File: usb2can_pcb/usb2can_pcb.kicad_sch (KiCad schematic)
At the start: 19 parts, among them J1 USB_C_Receptacle_USB2.0, J2 CAN, J3 CAN, U1 XC6206P332MR, U2 STM32F072C8T6, U3 MAX3051

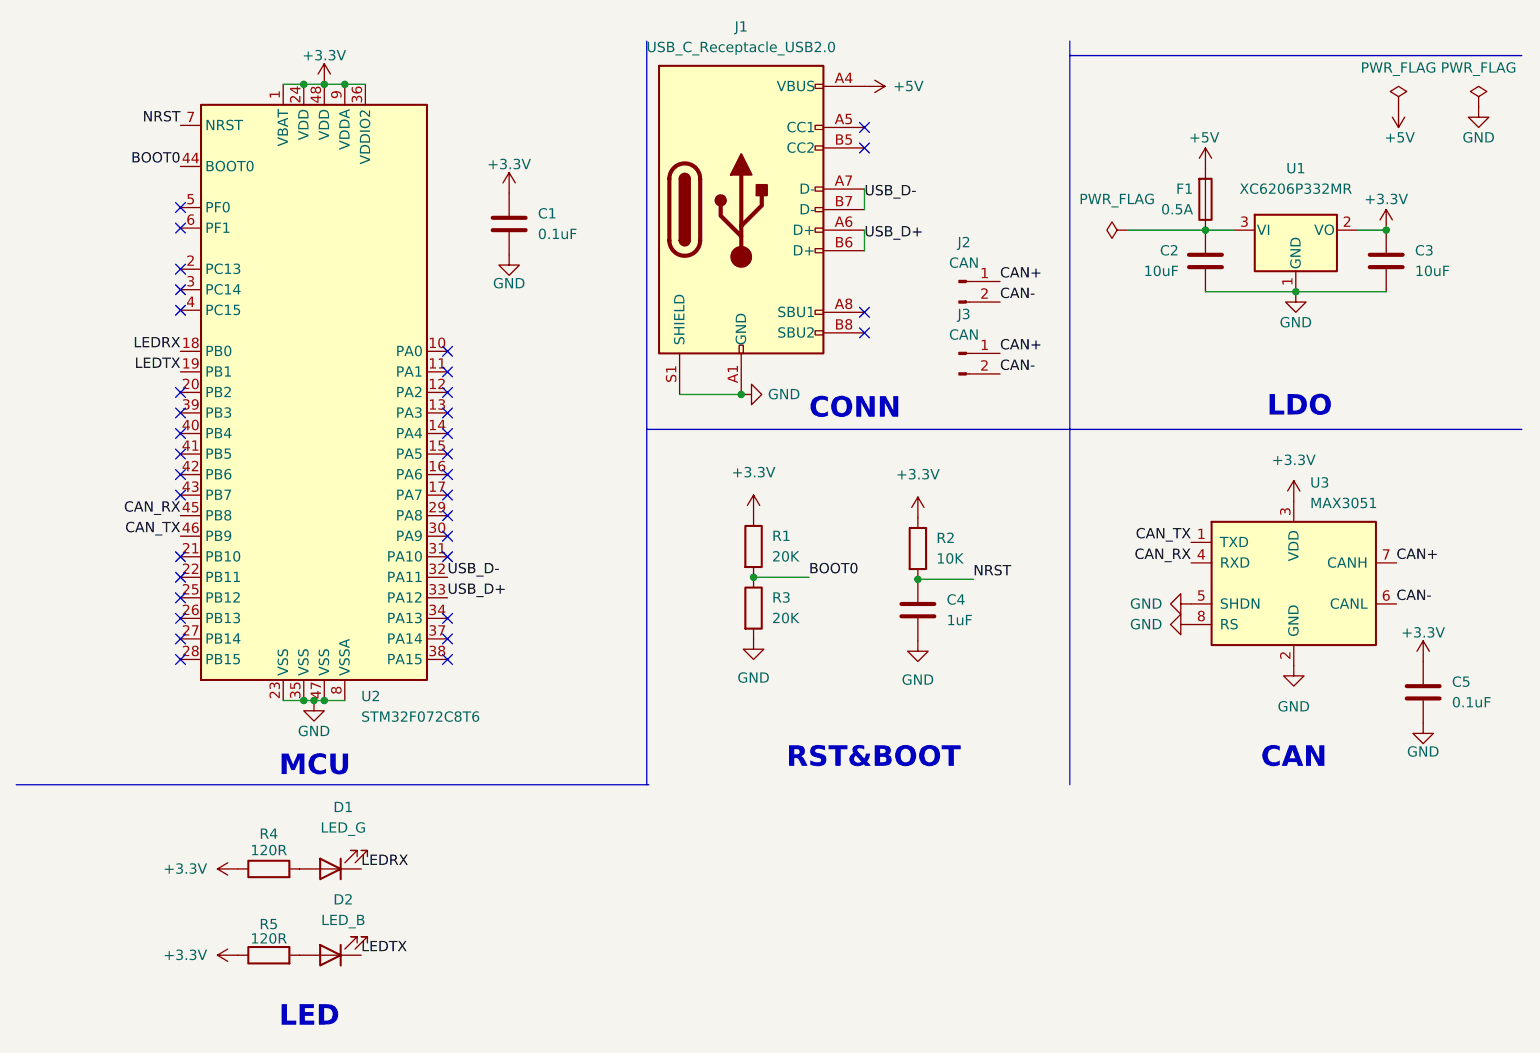
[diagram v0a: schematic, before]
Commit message: fix CAN connector pin assign problem
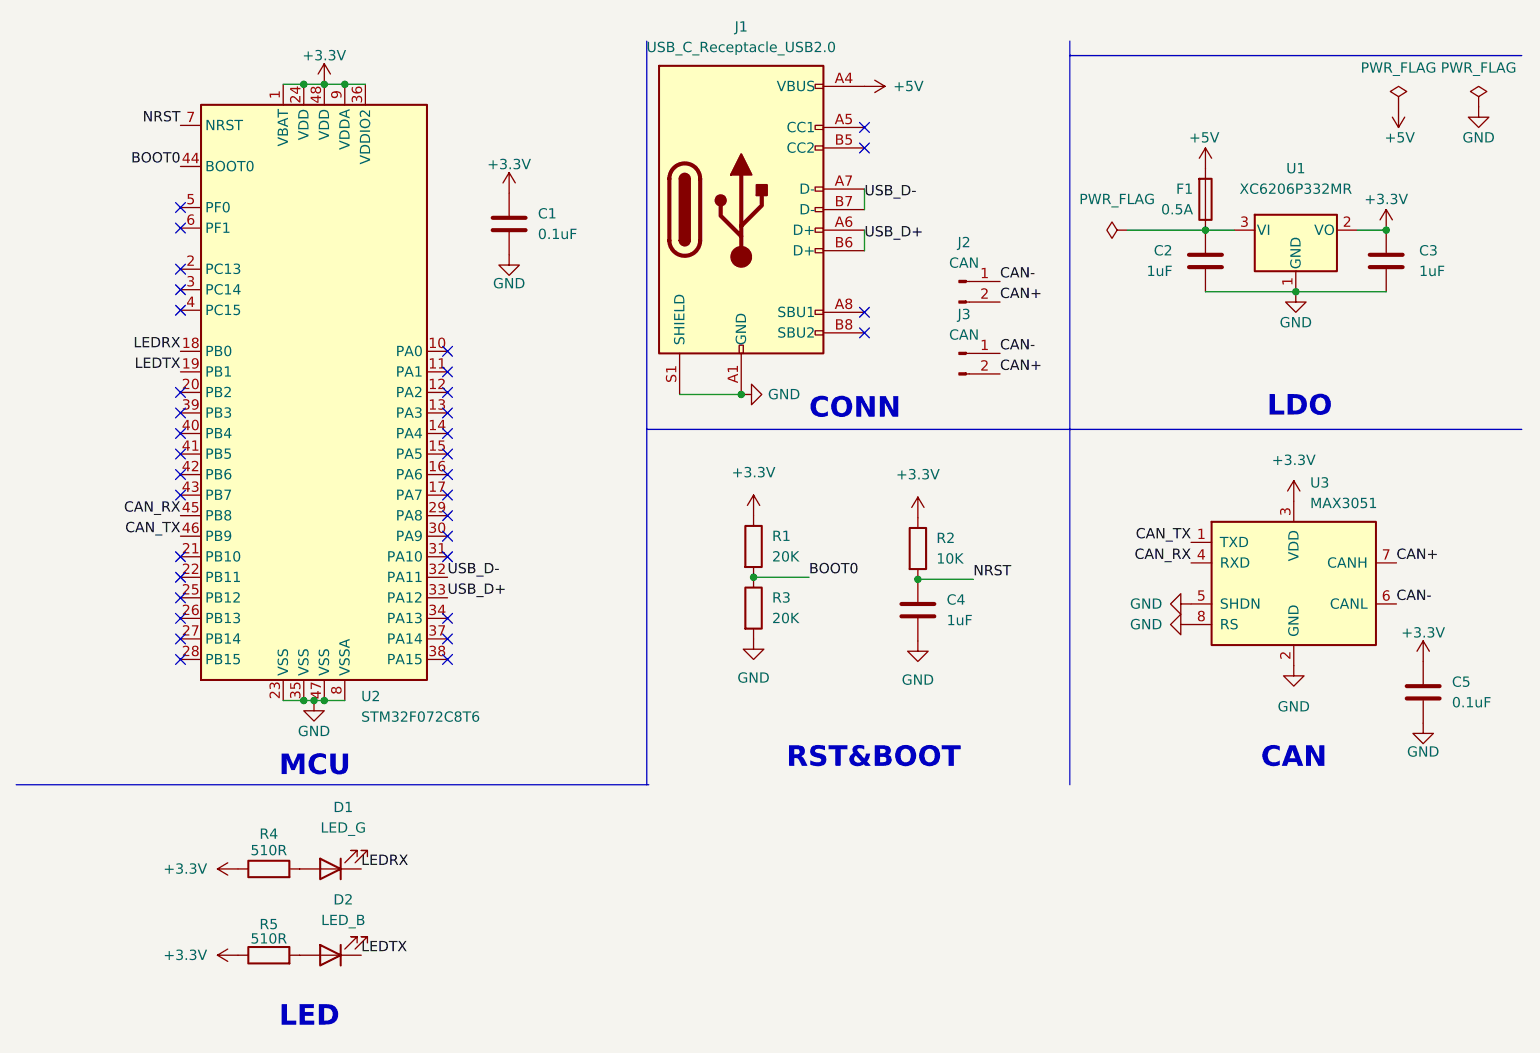
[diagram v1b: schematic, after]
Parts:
- C2, C3: value 10uF -> 1uF
- R4, R5: value 120R -> 510R
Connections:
- net CAN+: now also J2.2 (Pin_2), J3.2 (Pin_2); no longer J2.1 (Pin_1), J3.1 (Pin_1)
- net CAN-: now also J2.1 (Pin_1), J3.1 (Pin_1); no longer J2.2 (Pin_2), J3.2 (Pin_2)
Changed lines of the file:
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@@
     (effects (font (size 1.27 1.27)) (justify right bottom))
   )
-  (label "CAN-" (at 133.604 44.196 0)
+  (label "CAN-" (at 133.604 41.656 0)
     (effects (font (size 1.27 1.27)) (justify left bottom))
   )
@@
     (effects (font (size 1.27 1.27)) (justify left bottom))
   )
-  (label "CAN+" (at 133.604 41.656 0)
+  (label "CAN+" (at 133.604 44.196 0)
     (effects (font (size 1.27 1.27)) (justify left bottom))
   )
@@
     (effects (font (size 1.27 1.27)) (justify right bottom))
   )
-  (label "CAN-" (at 133.604 53.086 0)
+  (label "CAN-" (at 133.604 50.546 0)
     (effects (font (size 1.27 1.27)) (justify left bottom))
   )
@@
     (effects (font (size 1.27 1.27)) (justify right bottom))
   )
-  (label "CAN+" (at 133.604 50.546 0)
+  (label "CAN+" (at 133.604 53.086 0)
     (effects (font (size 1.27 1.27)) (justify left bottom))
   )
@@
   (symbol (lib_id "Device:C") (at 181.356 39.116 0) (mirror y) (unit 1)
     (in_bom yes) (on_board yes) (fields_autoplaced)
-    (property "Reference" "C3" (id 0) (at 184.912 37.8459 0)
+    (property "Reference" "C3" (id 0) (at 185.42 37.8459 0)
       (effects (font (size 1.27 1.27)) (justify right))
     )
-    (property "Value" "10uF" (id 1) (at 184.912 40.3859 0)
+    (property "Value" "1uF" (id 1) (at 185.42 40.3859 0)
       (effects (font (size 1.27 1.27)) (justify right))
     )
@@
   (symbol (lib_id "Device:C") (at 159.004 39.116 0) (mirror x) (unit 1)
     (in_bom yes) (on_board yes) (fields_autoplaced)
-    (property "Reference" "C2" (id 0) (at 155.702 37.8459 0)
+    (property "Reference" "C2" (id 0) (at 154.94 37.8459 0)
       (effects (font (size 1.27 1.27)) (justify right))
     )
-    (property "Value" "10uF" (id 1) (at 155.702 40.3859 0)
+    (property "Value" "1uF" (id 1) (at 154.94 40.3859 0)
       (effects (font (size 1.27 1.27)) (justify right))
     )
@@
     (in_bom yes) (on_board yes)
     (property "Reference" "R5" (id 0) (at 43.18 121.158 90))
-    (property "Value" "120R" (id 1) (at 43.18 122.936 90))
+    (property "Value" "510R" (id 1) (at 43.18 122.936 90))
     (property "Footprint" "Resistor_SMD:R_0402_1005Metric" (id 2) (at 43.18 126.746 90)
       (effects (font (size 1.27 1.27)) hide)
@@
     (in_bom yes) (on_board yes)
     (property "Reference" "R4" (id 0) (at 43.18 109.982 90))
-    (property "Value" "120R" (id 1) (at 43.18 112.014 90))
+    (property "Value" "510R" (id 1) (at 43.18 112.014 90))
     (property "Footprint" "Resistor_SMD:R_0402_1005Metric" (id 2) (at 43.18 116.078 90)
       (effects (font (size 1.27 1.27)) hide)
@@
     )
     (path "/892c21e4-a765-485b-b841-bbcd8288c811"
-      (reference "C2") (unit 1) (value "10uF") (footprint "Capacitor_SMD:C_0402_1005Metric")
+      (reference "C2") (unit 1) (value "1uF") (footprint "Capacitor_SMD:C_0402_1005Metric")
     )
     (path "/1a895f1e-bd8b-4e1b-8824-e295ac41388c"
-      (reference "C3") (unit 1) (value "10uF") (footprint "Capacitor_SMD:C_0402_1005Metric")
+      (reference "C3") (unit 1) (value "1uF") (footprint "Capacitor_SMD:C_0402_1005Metric")
     )
     (path "/db1f3c30-d9a1-431f-b2be-64a99036ca26"
@@
     )
     (path "/ab331e7a-e244-4f94-b655-f577af721049"
-      (reference "R4") (unit 1) (value "120R") (footprint "Resistor_SMD:R_0402_1005Metric")
+      (reference "R4") (unit 1) (value "510R") (footprint "Resistor_SMD:R_0402_1005Metric")
     )
     (path "/89a44c6b-8780-46f1-96a2-e6fb7c0338c6"
-      (reference "R5") (unit 1) (value "120R") (footprint "Resistor_SMD:R_0402_1005Metric")
+      (reference "R5") (unit 1) (value "510R") (footprint "Resistor_SMD:R_0402_1005Metric")
     )
     (path "/5fc14624-14dc-40af-9cf8-c7acd716afa8"
